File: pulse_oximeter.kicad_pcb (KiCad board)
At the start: 2 copper layers, 78 x 79.5 mm, 93 parts, among them SW1 SW_Omron_B3FS, SW2 SW_Omron_B3FS, SW3 SW_Omron_B3FS, X1 FT232RL, X2 Conn_01x03

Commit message: Посадочные места в библиотеке (GOST_FP), правила DRC «Резонит», отчёт по пунктам задания
Co-Authored-By: Claude Opus 5.5 <noreply@anthropic.com>
Claude-Session: https://claude.ai/code/session_01FsJMMwHQ3FuEgyASHhQBd4
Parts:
- C1, C10, C11, C12, C13, C14, C15, C16, C17, C18, C19, C2, C20, C21, C22, C23, C24, C25, C26, C27, C3, C33, C4, C49, C5, C6, C7, C8, C9: footprint Capacitor_THT:C_Disc_D5.1mm_W3.2mm_P5.00mm -> GOST_FP:C_Disc_D5.1mm_W3.2mm_P5.00mm
- DA1, DA2, DA3, DA4, DA5, DA6, DA7: footprint Package_DIP:DIP-8_W7.62mm -> GOST_FP:DIP-8_W7.62mm
- DA16: footprint Package_TO_SOT_THT:TO-220-3_Vertical -> GOST_FP:TO-220-3_Vertical
- DA8: footprint Package_DIP:DIP-16_W7.62mm -> GOST_FP:DIP-16_W7.62mm
- DD1: footprint Package_QFP:LQFP-48_7x7mm_P0.5mm -> GOST_FP:LQFP-48_7x7mm_P0.5mm
- HL1, HL2: footprint OptoDevice:LaserDiode_TO18-D5.6-3 -> GOST_FP:LaserDiode_TO18-D5.6-3
- R1, R10, R11, R12, R14, R15, R16, R17, R18, R2, R21, R22, R23, R24, R25, R26, R27, R28, R3, R30, R31, R34, R35, R4, R40, R42, R43, R5, R6, R62, R63, R7, R8, R9: footprint Resistor_THT:R_Axial_DIN0309_L9.0mm_D3.2mm_P2.54mm_Vertical -> GOST_FP:R_Axial_DIN0309_L9.0mm_D3.2mm_P2.54mm_Vertical
- R13, R19, R20, R29, R37, R44: footprint Potentiometer_THT:Potentiometer_Bourns_3296W_Vertical -> GOST_FP:Potentiometer_Bourns_3296W_Vertical
- SW1, SW2, SW3: footprint Button_Switch_THT:SW_PUSH_6mm -> GOST_FP:SW_PUSH_6mm
- VD1: footprint OptoDevice:Osram_DIL2_4.3x4.65mm_P5.08mm -> GOST_FP:Osram_DIL2_4.3x4.65mm_P5.08mm
- VD2, VD3, VD4, VD5: footprint Diode_THT:D_DO-41_SOD81_P10.16mm_Horizontal -> GOST_FP:D_DO-41_SOD81_P10.16mm_Horizontal
- VT1, VT2: footprint Package_TO_SOT_THT:TO-126-3_Vertical -> GOST_FP:TO-126-3_Vertical
- X1: footprint Package_SO:SSOP-28_5.3x10.2mm_P0.65mm -> GOST_FP:SSOP-28_5.3x10.2mm_P0.65mm
- X2: footprint Connector_PinHeader_2.54mm:PinHeader_1x03_P2.54mm_Vertical -> GOST_FP:PinHeader_1x03_P2.54mm_Vertical

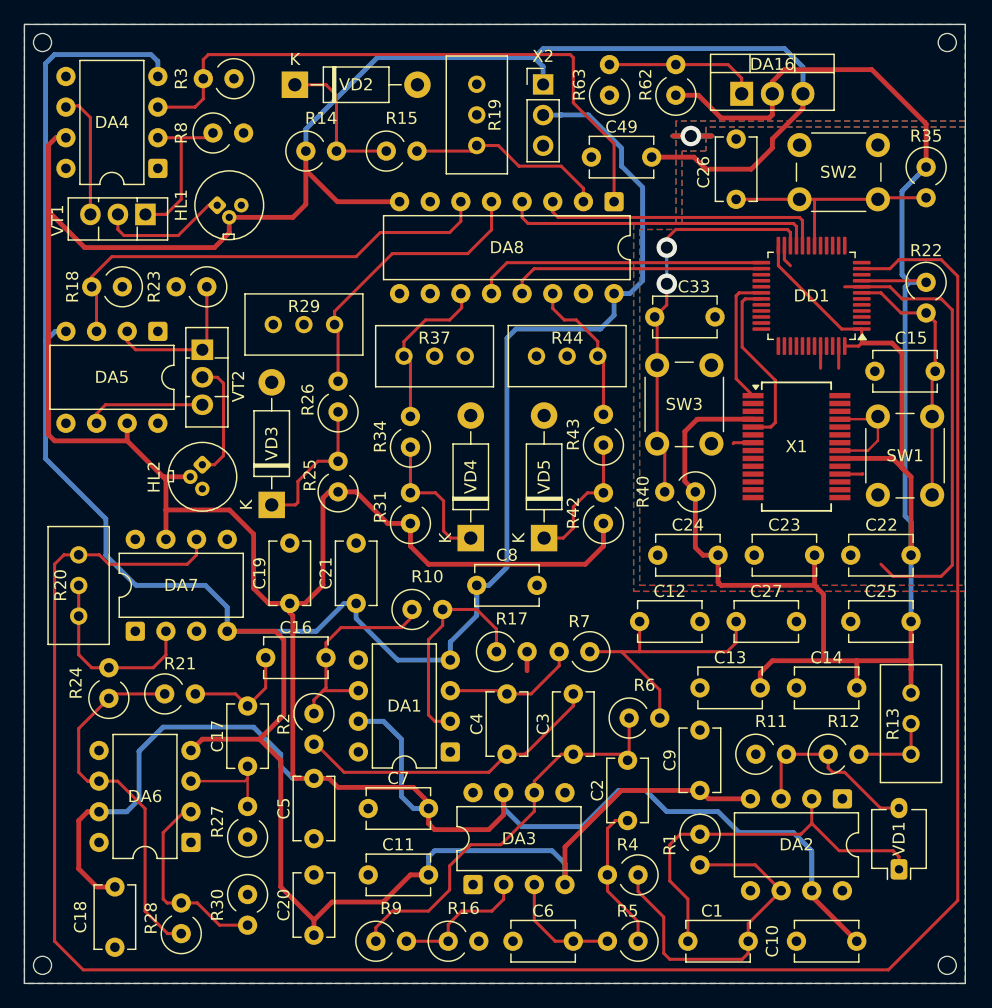
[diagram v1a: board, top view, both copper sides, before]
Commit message: Итоговая версия проекта: схема и плата после трассировки, все УГО и посадочные места из библиотеки, ERC/DRC без ошибок, STEP в скрипте, отчёт обновлён
Co-Authored-By: Claude Opus 5.5 <noreply@anthropic.com>
Claude-Session: https://claude.ai/code/session_01FsJMMwHQ3FuEgyASHhQBd4
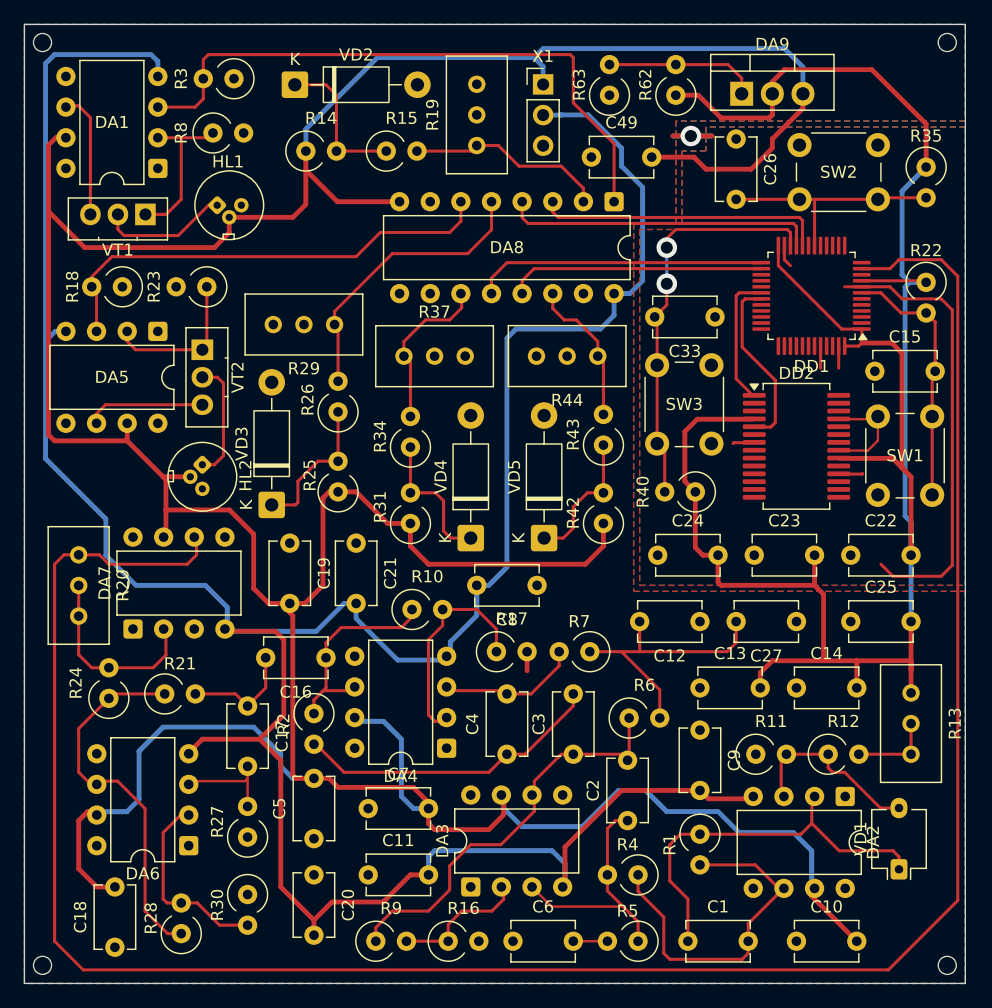
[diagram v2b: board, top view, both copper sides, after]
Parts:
- removed the DA1 at (99.3, 101.8)
- removed the X1 at (128.0, 76.5)
- added DA4: OPA340P, GOST_FP:DIP-8_W7.62mm, F.Cu at (99.0, 101.5)
- added DD2: FT232RL, GOST_FP:SSOP-28_5.3x10.2mm_P0.65mm, F.Cu at (128.0, 76.5)
- C1, C10, C11, C12, C13, C14, C15, C16, C17, C18, C19, C2, C20, C21, C22, C23, C24, C25, C26, C27, C3, C33, C4, C49, C5, C6, C7, C8, C9: value C -> 100n
- DA8: value ~ -> КР590КН2
- DA9: renamed from DA16; value LM1117MP-ADJ -> LM1117T-ADJ
- DD1: value STM32F030C8Tx -> STM32F030C8T6
- HL1, HL2: value LED -> TSAL6200
- R1, R11, R12, R18, R21, R23, R28, R4, R5, R6, R62, R7: value R -> 10k
- R10, R16, R17, R2, R22, R3, R35, R40, R9: value 22к -> 22k
- R13, R19, R20, R29, R37, R44: value R_Potentiometer -> 10k
- R14, R24, R25, R27, R30, R31, R42, R63, R8: value 400 -> 390
- SW1, SW2, SW3: value SW_Omron_B3FS -> B3F-1000
- VD2, VD3, VD4, VD5: value ZYxxx -> 5V1
- VT1, VT2: value BD235 -> BD139-16
- moved DA6 0.33 mm to (77.6, 109.6)
- moved DA2 0.30 mm to (132.0, 105.5)
- moved DA3 0.27 mm to (101.0, 113.0)
- moved DA7 0.27 mm to (73.0, 91.6)
- renumbered DA4 to DA1, X2 to X1
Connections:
- net Net-(C1-Pad2) renamed /TIA_OUT
- net Net-(C16-Pad1) renamed /NOTCH_OUT
- net Net-(C2-Pad2) renamed /LPF_OUT
- net Net-(DA2-+) renamed /PD_A
- net Net-(DA2--) renamed /PD_K
- net Net-(DA4-+) renamed /LED1_REF
- net Net-(DA5-+) renamed /LED2_REF
- net Net-(DA6-Pad6) renamed /HPF_OUT
- net Net-(DA8-IN1) renamed /REF1
- net Net-(DA8-IN2) renamed /REF2
- net Net-(DA8-IN3) renamed /REF3
- net Net-(DA8-IN4) renamed /REF4
- net Net-(DD1-NRST) renamed /NRST
- net Net-(DD1-PB0) renamed /BTN1
- net Net-(DD1-PB11) renamed /BTN2
- net В10 renamed /SW_D2
- net В12 renamed /SW_D3
- net В13 renamed /SW_D4
- net В2 renamed /SW_D1
- net Г renamed /ADC_IN
- C6 pad 2: Net-(DA3-+) -> Net-(C6-Pad2)
- DA3 pad 3: Net-(DA3-+) -> Net-(C2-Pad1)
- DD1 pad 12: Д -> unconnected-(DD1-PA2-Pad12)
- DD1 pad 13: Е -> unconnected-(DD1-PA3-Pad13)
- DD1 pad 14: Ж -> unconnected-(DD1-PA4-Pad14)
- DD1 pad 16: З -> unconnected-(DD1-PA6-Pad16)
- DD1 pad 30: Net-(DD1-PA9) -> /UART_TX
- DD1 pad 31: Net-(DD1-PA10) -> /UART_RX
- R5 pad 2: Net-(DA3-+) -> Net-(C6-Pad2)
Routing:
- net Net-(DD1-PA10): track 14.8 -> 0.00 mm
- net /UART_RX: track 0.00 -> 14.8 mm
- net Net-(DD1-PA9): track 11.0 -> 0.00 mm
- net /UART_TX: track 0.00 -> 11.0 mm
- net Net-(DA3-+): track 9.74 -> 0.00 mm
- net Net-(C2-Pad1): track 12.3 -> 20.6 mm
- net Net-(C6-Pad2): track 0.00 -> 2.83 mm
